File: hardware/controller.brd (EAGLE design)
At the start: 98 x 71 mm, 44 parts, among them J1 AVR_SPI_PRG_6NS, J10 22-27-2041-04, J11 22-27-2041-04, J2 ATX24RH, J3 22-27-2041-04, J4 22-27-2041-04, J5 22-27-2021-02, J6 22-27-2021-02, J7 22-27-2031-03, J8 22-27-2041-04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

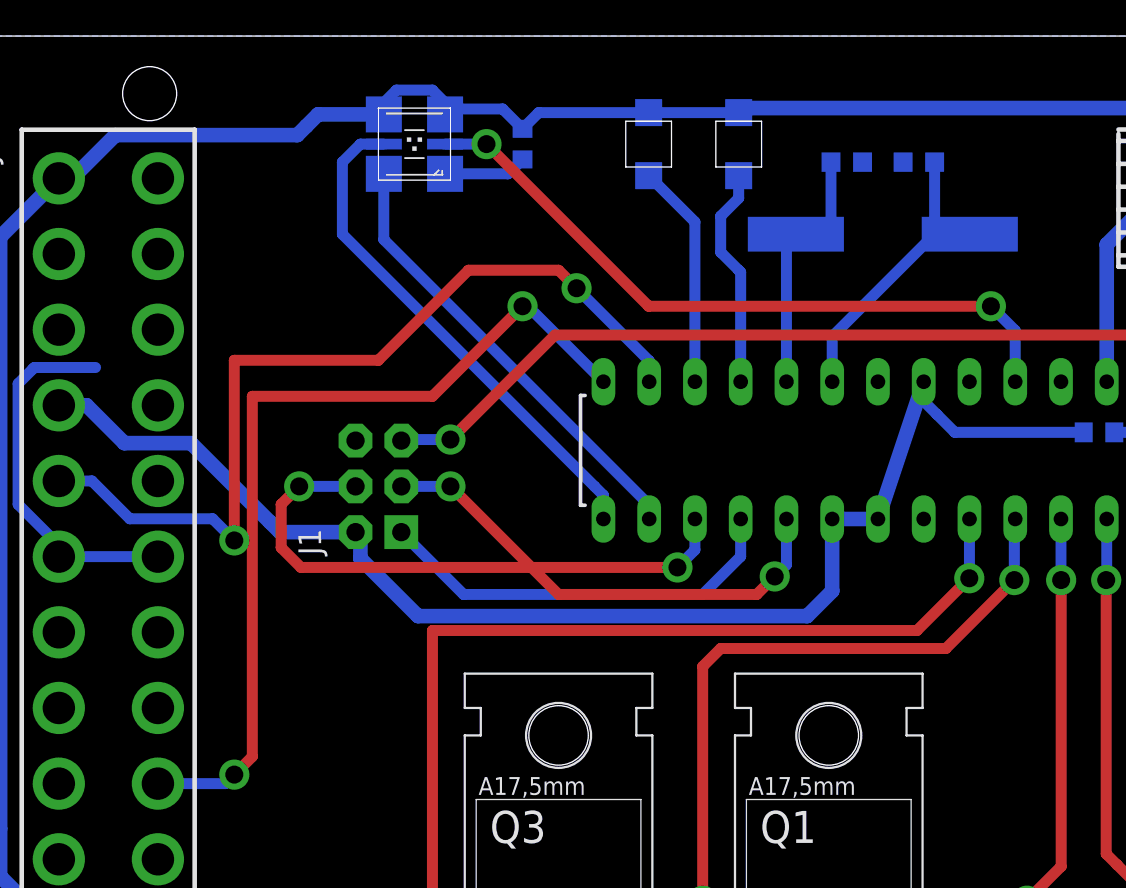
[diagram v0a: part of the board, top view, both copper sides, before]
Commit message: Hardware: Add fourth hole and different crystal footprint.
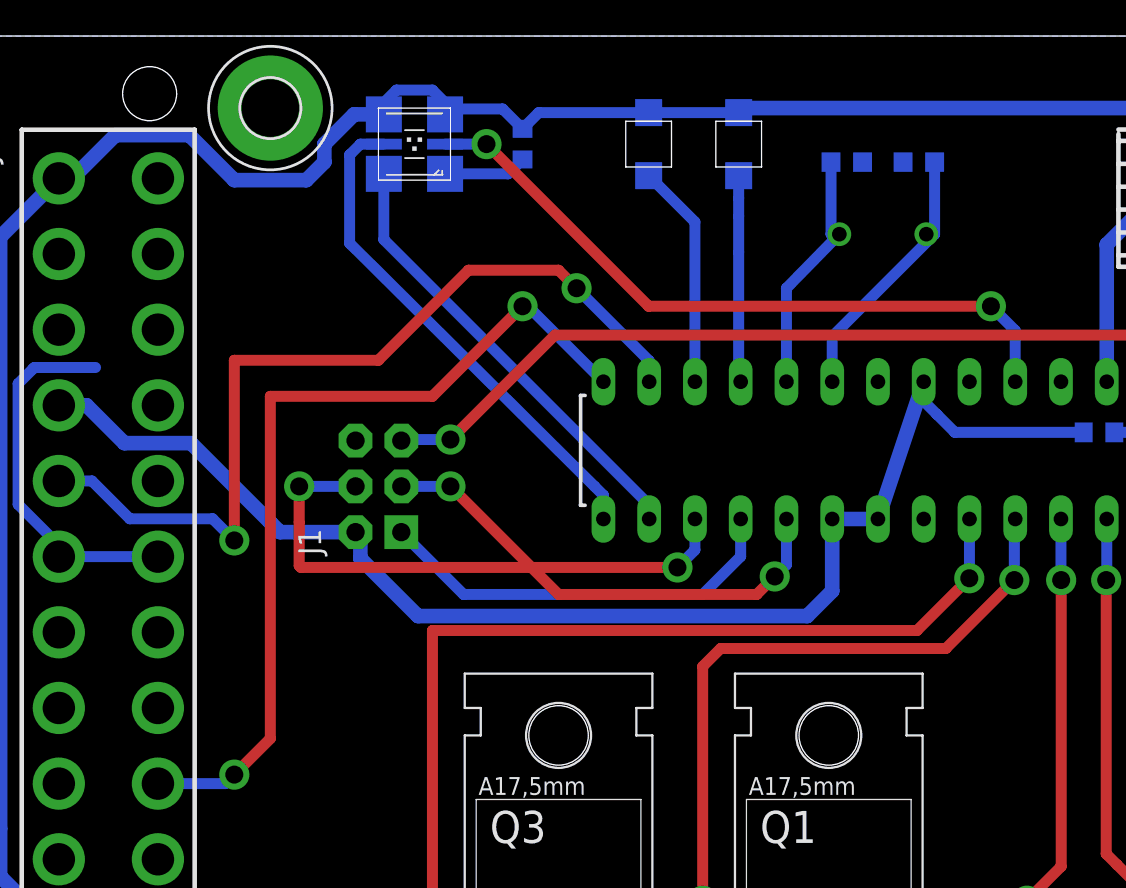
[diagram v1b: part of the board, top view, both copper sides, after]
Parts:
- added H4: MOUNT-PAD-ROUND3.2, holes:3,2-PAD
- Y1: device SparkFun-FreqCtrl:HC49UP -> SparkFun-FreqCtrl:HC49U-V
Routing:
- net +3V3: track 235.3 -> 237.9 mm
- net N$1: track 16.5 -> 15.0 mm
- net LED1: track 12.3 -> 11.5 mm
- net MOSI: track 32.5 -> 31.7 mm
- net N$2: track 14.7 -> 13.9 mm
- net PS_ON: track 49.2 -> 48.6 mm
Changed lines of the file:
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@@
 <element name="U1" library="SparkFun-DigitalIC" package="DIL28-3" value="ATMEGA328P_PDIP" x="51" y="48" rot="R180"/>
 <element name="J1" library="SparkFun-Connectors" package="2X3-NS" value="AVR_SPI_PRG_6NS" x="22" y="46" rot="R90"/>
-<element name="Y1" library="SparkFun-FreqCtrl" package="HC49UP" value="" x="50" y="60" rot="MR180"/>
+<element name="Y1" library="SparkFun-FreqCtrl" package="HC49U-V" value="" x="50" y="60" rot="MR180"/>
 <element name="Q1" library="transistor-fet" package="TO220" value="BUZ11" x="47" y="21"/>
 <element name="D1" library="diode" package="DO201-15" value="" x="54" y="11" rot="R90"/>
@@
 <element name="H3" library="holes" package="3,2-PAD" value="MOUNT-PAD-ROUND3.2" x="93" y="66"/>
 <element name="R13" library="rcl" package="R0603" value="1k" x="62" y="49" rot="MR180"/>
+<element name="H4" library="holes" package="3,2-PAD" value="MOUNT-PAD-ROUND3.2" x="16" y="67"/>
 </elements>
 <signals>
@@
 <contactref element="Y1" pad="2"/>
 <contactref element="C3" pad="2"/>
-<wire x1="54.826" y1="60" x2="52.875" y2="60" width="0.6096" layer="16"/>
+<wire x1="52.413" y1="60" x2="52.875" y2="60" width="0.6096" layer="16"/>
 <wire x1="52.875" y1="60" x2="52.875" y2="64" width="0.6096" layer="16"/>
 <wire x1="52.875" y1="60" x2="47.19" y2="54.315" width="0.6096" layer="16"/>
@@
 <contactref element="Y1" pad="1"/>
 <contactref element="C4" pad="2"/>
-<wire x1="45.174" y1="60" x2="47.125" y2="60" width="0.6096" layer="16"/>
+<wire x1="47.587" y1="60" x2="47.125" y2="60" width="0.6096" layer="16"/>
 <wire x1="47.125" y1="60" x2="47.125" y2="64" width="0.6096" layer="16"/>
-<wire x1="45.174" y1="60" x2="44.65" y2="60" width="0.6096" layer="16"/>
-<wire x1="44.65" y1="60" x2="44.65" y2="51.81" width="0.6096" layer="16"/>
+<wire x1="47.587" y1="60" x2="44.65" y2="57" width="0.6096" layer="16"/>
+<wire x1="44.65" y1="57" x2="44.65" y2="51.81" width="0.6096" layer="16"/>
 </signal>
 <signal name="MISO">
@@
 <via x="38.6" y="41.5" extent="1-16" drill="1" diameter="1.6764"/>
 <wire x1="38.6" y1="41.5" x2="17.7" y2="41.5" width="0.6096" layer="1"/>
-<wire x1="17.7" y1="41.5" x2="16.6" y2="42.6" width="0.6096" layer="1"/>
-<wire x1="16.6" y1="42.6" x2="16.6" y2="45" width="0.6096" layer="1"/>
-<wire x1="16.6" y1="45" x2="17.6" y2="46" width="0.6096" layer="1"/>
+<wire x1="17.7" y1="41.5" x2="17.6" y2="41.6" width="0.6096" layer="1"/>
+<wire x1="17.6" y1="41.6" x2="17.6" y2="44" width="0.6096" layer="1"/>
+<wire x1="17.6" y1="44" x2="17.6" y2="46" width="0.6096" layer="1"/>
 <via x="17.6" y="46" extent="1-16" drill="1" diameter="1.6764"/>
 <wire x1="17.6" y1="46" x2="20.73" y2="46" width="0.6096" layer="16"/>
@@
 <wire x1="4.26" y1="63.1" x2="5" y2="63.1" width="0.8128" layer="16"/>
 <wire x1="5" y1="63.1" x2="7.4" y2="65.5" width="0.8128" layer="16"/>
-<wire x1="7.4" y1="65.5" x2="17.5" y2="65.5" width="0.8128" layer="16"/>
-<wire x1="17.5" y1="65.5" x2="18" y2="66" width="0.8128" layer="16"/>
-<wire x1="18" y1="66" x2="18.65" y2="66.65" width="0.8128" layer="16"/>
-<wire x1="18.65" y1="66.65" x2="22.3" y2="66.65" width="0.8128" layer="16"/>
+<wire x1="7.4" y1="65.5" x2="11.5" y2="65.5" width="0.8128" layer="16"/>
+<wire x1="11.5" y1="65.5" x2="14" y2="63" width="0.8128" layer="16"/>
+<wire x1="14" y1="63" x2="18" y2="63" width="0.8128" layer="16"/>
+<wire x1="18" y1="63" x2="19" y2="64" width="0.8128" layer="16"/>
+<wire x1="19" y1="64" x2="19" y2="65" width="0.8128" layer="16"/>
+<wire x1="19" y1="65" x2="20.65" y2="66.65" width="0.8128" layer="16"/>
+<wire x1="20.65" y1="66.65" x2="22.3" y2="66.65" width="0.8128" layer="16"/>
 <wire x1="9.76" y1="16.9" x2="4.26" y2="16.9" width="0.8128" layer="16"/>
 <wire x1="4.26" y1="16.9" x2="4.26" y2="21.1" width="0.8128" layer="16"/>
@@
 <contactref element="U1" pad="15"/>
 <wire x1="22.3" y1="65" x2="21" y2="65" width="0.6096" layer="16"/>
-<wire x1="21" y1="65" x2="20" y2="64" width="0.6096" layer="16"/>
-<wire x1="20" y1="64" x2="20" y2="60" width="0.6096" layer="16"/>
-<wire x1="20" y1="60" x2="34" y2="46" width="0.6096" layer="16"/>
+<wire x1="21" y1="65" x2="20.4" y2="64.4" width="0.6096" layer="16"/>
+<wire x1="20.4" y1="64.4" x2="20.4" y2="59.5" width="0.6096" layer="16"/>
+<wire x1="20.4" y1="59.5" x2="34" y2="46" width="0.6096" layer="16"/>
 <wire x1="34" y1="46" x2="34.49" y2="45.51" width="0.6096" layer="16"/>
 <wire x1="34.49" y1="45.51" x2="34.49" y2="44.19" width="0.6096" layer="16"/>
@@
 <contactref element="U1" pad="11"/>
 <wire x1="42" y1="63.25" x2="42" y2="62" width="0.6096" layer="16"/>
-<wire x1="42" y1="62" x2="41" y2="61" width="0.6096" layer="16"/>
-<wire x1="41" y1="61" x2="41" y2="59" width="0.6096" layer="16"/>
-<wire x1="41" y1="59" x2="42" y2="58" width="0.6096" layer="16"/>
-<wire x1="42.11" y1="51.81" x2="42.11" y2="57.89" width="0.6096" layer="16"/>
-<wire x1="42.11" y1="57.89" x2="42" y2="58" width="0.6096" layer="16"/>
+<wire x1="42" y1="62" x2="42" y2="61" width="0.6096" layer="16"/>
+<wire x1="42" y1="61" x2="42" y2="59" width="0.6096" layer="16"/>
+<wire x1="42" y1="59" x2="42" y2="52" width="0.6096" layer="16"/>
+<wire x1="42.11" y1="51.81" x2="42.11" y2="51.89" width="0.6096" layer="16"/>
+<wire x1="42.11" y1="51.89" x2="42" y2="52" width="0.6096" layer="16"/>
 </signal>
 <signal name="LED2">
@@
 <via x="30" y="56" extent="1-16" drill="1" diameter="1.6764"/>
 <wire x1="30" y1="56" x2="25" y2="51" width="0.6096" layer="1"/>
-<wire x1="25" y1="51" x2="15" y2="51" width="0.6096" layer="1"/>
-<wire x1="15" y1="51" x2="15" y2="31" width="0.6096" layer="1"/>
-<wire x1="15" y1="31" x2="14" y2="30" width="0.6096" layer="1"/>
+<wire x1="25" y1="51" x2="16" y2="51" width="0.6096" layer="1"/>
+<wire x1="16" y1="51" x2="16" y2="32" width="0.6096" layer="1"/>
+<wire x1="16" y1="32" x2="14" y2="30" width="0.6096" layer="1"/>
 <via x="14" y="30" extent="1-16" drill="1" diameter="1.6764"/>
 <wire x1="14" y1="30" x2="13.5" y2="29.5" width="0.6096" layer="16"/>

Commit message: Update controller PCB.
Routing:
- net +12V: track 0.00 -> 76.6 mm
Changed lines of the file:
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@@
 <vertex x="16.9" y="0"/>
 </polygon>
+<wire x1="32.2" y1="2.2" x2="83.8" y2="2.2" width="3.81" layer="16"/>
+<wire x1="30" y1="4" x2="54" y2="4" width="3.81" layer="16"/>
+<wire x1="54" y1="4" x2="54" y2="3" width="3.81" layer="16"/>
+<wire x1="32" y1="3.19" x2="32.2" y2="2.2" width="0" layer="19" extent="16-16"/>
 </signal>
 <signal name="+3V3">

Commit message: Hardware: Redesign layout of controller PCB.
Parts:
- removed R4: 1k, rcl:R0603
- added C1, C2, C5, C6: (no value), rcl:C0603
- R1: value (none) -> 30
- U$1: device hauser:VSSOP8 -> hauser:MSOP8
- moved R3 36.7 mm to (78.7, 59.4), turned to 90 degrees
- moved H2 35.8 mm to (72.0, 34.0)
- moved U$1 34.5 mm to (81.1, 58.3), turned to 0 degrees
- moved J1 12.2 mm to (20.0, 34.0)
- moved H3 11.0 mm to (82.0, 66.0)
- moved LED1 7.00 mm to (31.0, 65.0), turned to 0 degrees
- moved C3 6.52 mm to (48.5, 58.5)
- moved C4 6.04 mm to (45.5, 58.5)
- moved R1 5.10 mm to (35.0, 66.0)
- moved Y1 4.24 mm to (47.0, 57.0)
- moved R13 1.71 mm to (60.4, 49.6)
- moved H4 1.00 mm to (16.0, 66.0)
- moved LED3 1.00 mm to (38.0, 65.0)
- turned J2 to 90 degrees
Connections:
- removed net N$8: R4.2, U$1.P$3
- net +3V3: now also C5.1, C6.1, R13.1, U$1.5, U$1.6, U$1.7, U$1.8; no longer R4.1, U$1.P$5, U$1.P$6, U$1.P$7, U$1.P$8
- net +5V: now also C1.1, C2.1; no longer R13.1
- net GND: now also C1.2, C2.2, C5.2, C6.2, U$1.4; no longer U$1.P$4
- net SCL: now also U$1.2; no longer U$1.P$2
- net SDA: now also U$1.1; no longer U$1.P$1
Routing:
- net +3V3: track 237.9 -> 196.1 mm, vias 2 -> 0
- net SCL: track 91.9 -> 66.4 mm, vias 2 -> 0
- net GND: track 79.1 -> 54.9 mm
- net SDA: track 90.0 -> 67.8 mm, vias 2 -> 0
- net !RESET: track 55.3 -> 72.4 mm
- net PS_ON: track 48.6 -> 32.5 mm, vias 2 -> 0
- net MISO: track 23.2 -> 36.9 mm
- net +5V: track 74.3 -> 63.9 mm
- net HEAT: track 55.6 -> 45.4 mm, vias 2 -> 0
- net COLD: track 42.0 -> 33.8 mm, vias 2 -> 0
- net N$1: track 15.0 -> 7.63 mm
- net N$2: track 13.9 -> 6.73 mm
- net N$8: track 6.67 -> 0.00 mm
- net BLUE: track 28.2 -> 21.6 mm
- net PWR_OK: track 49.5 -> 45.1 mm, vias 2 -> 0
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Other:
- board size 98 x 71 mm -> 87 x 71 mm

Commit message: Hardware: Add reset push button to PCB.
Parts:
- added S1: (no value), SparkFun-Electromechanical:TACTILE-PTH
- moved J7 2.00 mm to (64.0, 62.0)
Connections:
- net !RESET: now also S1.3, S1.4
- net GND: now also S1.1, S1.2
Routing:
- net !RESET: track 72.4 -> 82.0 mm
- net TXD: track 12.3 -> 13.1 mm
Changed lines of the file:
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@@
 <attribute name="OC_FARNELL" value="unknown" x="-0.47" y="-35.64" size="1.778" layer="27" rot="R270" display="off"/>
 </element>
-<element name="J7" library="con-molex" package="6410-03" value="22-27-2031-03" x="66" y="62" rot="R270">
-<attribute name="OC_NEWARK" value="unknown" x="-11.47" y="42.95" size="1.778" layer="27" rot="R270" display="off"/>
-<attribute name="MPN" value="" x="-11.47" y="42.95" size="1.778" layer="27" rot="R270" display="off"/>
-<attribute name="MF" value="" x="-11.47" y="42.95" size="1.778" layer="27" rot="R270" display="off"/>
-<attribute name="OC_FARNELL" value="unknown" x="-11.47" y="42.95" size="1.778" layer="27" rot="R270" display="off"/>
+<element name="J7" library="con-molex" package="6410-03" value="22-27-2031-03" x="64" y="62" rot="R270">
+<attribute name="OC_NEWARK" value="unknown" x="-13.47" y="42.95" size="1.778" layer="27" rot="R270" display="off"/>
+<attribute name="MPN" value="" x="-13.47" y="42.95" size="1.778" layer="27" rot="R270" display="off"/>
+<attribute name="MF" value="" x="-13.47" y="42.95" size="1.778" layer="27" rot="R270" display="off"/>
+<attribute name="OC_FARNELL" value="unknown" x="-13.47" y="42.95" size="1.778" layer="27" rot="R270" display="off"/>
 </element>
 <element name="J8" library="con-molex" package="6410-04" value="22-27-2041-04" x="81" y="26">
@@
 <element name="C5" library="rcl" package="C0603" value="" x="26" y="69" rot="MR270"/>
 <element name="C6" library="rcl" package="C0603" value="" x="50" y="63" rot="MR270"/>
+<element name="S1" library="SparkFun-Electromechanical" package="TACTILE-PTH" value="" x="71" y="58" rot="R270"/>
 </elements>
 <signals>
@@
 <vertex x="76" y="17"/>
 <vertex x="78" y="17"/>
-<vertex x="83" y="22"/>
-<vertex x="77.2" y="24"/>
+<vertex x="79" y="19"/>
+<vertex x="77.2" y="21"/>
 <vertex x="77.2" y="57"/>
 <vertex x="63" y="71"/>
@@
 <wire x1="53.4" y1="46.6" x2="53.2" y2="46.4" width="1.27" layer="16"/>
 <wire x1="53.2" y1="46.4" x2="53.2" y2="41.8" width="1.27" layer="16"/>
+<contactref element="S1" pad="1"/>
+<contactref element="S1" pad="2"/>
 </signal>
 <signal name="N$1">
@@
 </signal>
 <signal name="!RESET">
-<contactref element="U1" pad="1"/>
 <contactref element="J1" pad="5"/>
 <contactref element="R13" pad="2"/>
 <wire x1="61.25" y1="49.6" x2="66.6" y2="49.6" width="0.6096" layer="16"/>
 <wire x1="66.6" y1="49.6" x2="67.51" y2="50.51" width="0.6096" layer="16"/>
-<wire x1="67.51" y1="50.51" x2="67.51" y2="51.81" width="0.6096" layer="16"/>
 <wire x1="21.27" y1="36.54" x2="24.54" y2="36.54" width="0.6096" layer="16"/>
 <wire x1="24.54" y1="36.54" x2="26" y2="38" width="0.6096" layer="16"/>
@@
 <via x="71" y="50" extent="1-16" drill="1" diameter="1.27"/>
 <wire x1="71" y1="50" x2="69.32" y2="50" width="0.6096" layer="16"/>
-<wire x1="69.32" y1="50" x2="67.51" y2="51.81" width="0.6096" layer="16"/>
+<contactref element="S1" pad="4"/>
+<contactref element="S1" pad="3"/>
+<contactref element="U1" pad="1"/>
+<wire x1="68.7394" y1="61.2512" x2="68.7394" y2="54.7488" width="0.6096" layer="16"/>
+<wire x1="68.7394" y1="54.7488" x2="68.7394" y2="53.0394" width="0.6096" layer="16"/>
+<wire x1="68.7394" y1="53.0394" x2="67.51" y2="51.81" width="0.6096" layer="16"/>
+<wire x1="67.51" y1="51.81" x2="67.51" y2="51" width="0.6096" layer="16"/>
+<wire x1="67.51" y1="51" x2="67.51" y2="50.51" width="0.6096" layer="16"/>
+<wire x1="69.32" y1="50" x2="68.51" y2="50" width="0.6096" layer="16"/>
+<wire x1="68.51" y1="50" x2="67.51" y2="51" width="0.6096" layer="16"/>
 </signal>
 <signal name="RXD">
@@
 <contactref element="J7" pad="1"/>
 <wire x1="64.97" y1="51.81" x2="64.97" y2="58.43" width="0.8128" layer="16"/>
-<wire x1="64.97" y1="58.43" x2="66" y2="59.46" width="0.8128" layer="16"/>
+<wire x1="64.97" y1="58.43" x2="64" y2="59.46" width="0.8128" layer="16"/>
 </signal>
 <signal name="TXD">
 <contactref element="U1" pad="3"/>
 <contactref element="J7" pad="2"/>
-<wire x1="62.43" y1="51.81" x2="62.43" y2="59.43" width="0.8128" layer="16"/>
-<wire x1="62.43" y1="59.43" x2="65" y2="62" width="0.8128" layer="16"/>
-<wire x1="65" y1="62" x2="66" y2="62" width="0.8128" layer="16"/>
+<wire x1="62.43" y1="51.81" x2="62.43" y2="52.57" width="0.8128" layer="16"/>
+<wire x1="62.43" y1="52.57" x2="60.4" y2="54.6" width="0.8128" layer="16"/>
+<wire x1="60.4" y1="54.6" x2="60.43" y2="59.43" width="0.8128" layer="16"/>
+<wire x1="60.43" y1="59.43" x2="63" y2="62" width="0.8128" layer="16"/>
+<wire x1="63" y1="62" x2="64" y2="62" width="0.8128" layer="16"/>
 </signal>
 <signal name="SCL">
